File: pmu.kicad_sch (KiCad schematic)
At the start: 18 parts, among them J4 Battery, SW1 POWER ON/OFF, U3 MAX1555, U4 MAX16054, U5 TPS63030DSK

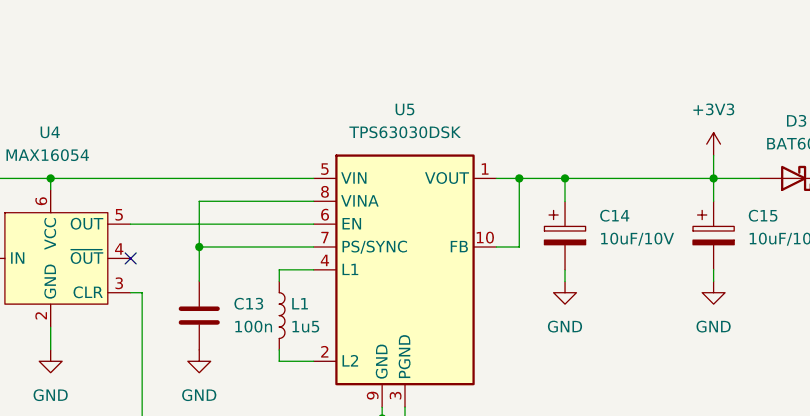
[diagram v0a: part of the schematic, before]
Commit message: U5 value update
TPS63030 is a regulated version of the 3.3V TPS63031. The latter is correct.
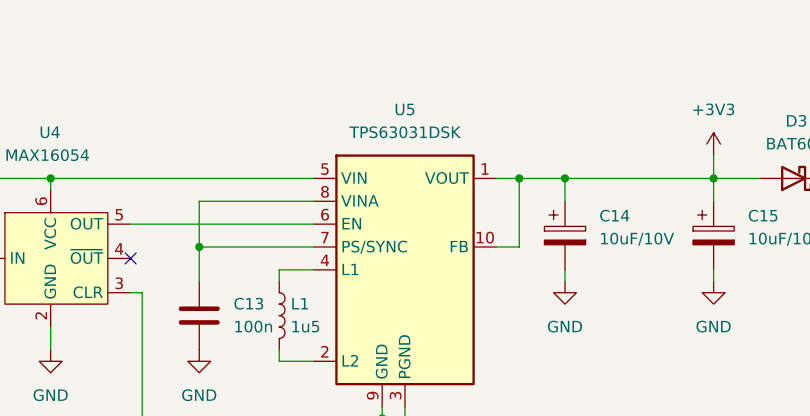
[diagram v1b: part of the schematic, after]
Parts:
- U5: value TPS63030DSK -> TPS63031DSK; MPN 595-TPS63030DSKR -> 595-TPS63031DSKR; PN 595-TPS63030DSKR -> 595-TPS63031DSKR
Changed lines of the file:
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@@
 	(title_block
 		(title "Mainboard replacement for Nokia 3310")
-		(date "23-11-2024")
+		(date "13-12-2024")
 		(rev "Rev A")
 		(company "M17 Project")
@@
 			)
 		)
-		(property "Value" "TPS63030DSK"
+		(property "Value" "TPS63031DSK"
 			(at 170.18 78.74 0)
 			(effects
@@
 			)
 		)
-		(property "MPN" "595-TPS63030DSKR"
+		(property "MPN" "595-TPS63031DSKR"
 			(at 170.18 93.98 0)
 			(effects
@@
 			)
 		)
-		(property "PN" "595-TPS63030DSKR"
+		(property "PN" "595-TPS63031DSKR"
 			(at 170.18 93.98 0)
 			(effects
